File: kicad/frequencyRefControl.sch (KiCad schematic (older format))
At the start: 15 parts, among them J83 Conn_01x01_Male, J84 Conn_01x01_Male, J85 Conn_01x01_Male

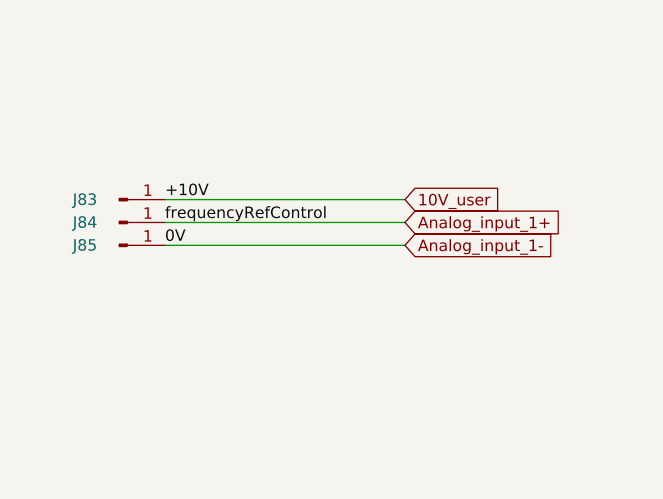
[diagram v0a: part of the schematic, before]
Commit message: KICAD: Agregar cambios esquemáticos
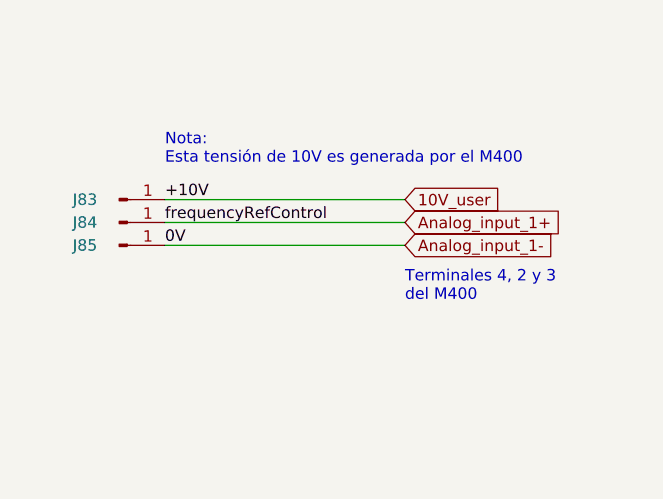
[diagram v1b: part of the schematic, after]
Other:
- note added: "Nota:\nEsta tensión de 10V es generada por el M400"
- note added: "Terminales 4, 2 y 3 \ndel M400"
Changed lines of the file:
@@
 Sheet 18 22
 Title "Mainet-mega -- frequencyRefControl"
-Date "2021-04-07"
+Date "2021-06-18"
 Rev "1.0"
 Comp "Tovenca"
@@
 Wire Wire Line
 	9050 3650 10100 3650
+Text Notes 10100 3900 0    50   ~ 0
+Terminales 4, 2 y 3 \ndel M400
+Text Notes 9050 3300 0    50   ~ 0
+Nota:\nEsta tensión de 10V es generada por el M400
 $EndSCHEMATC

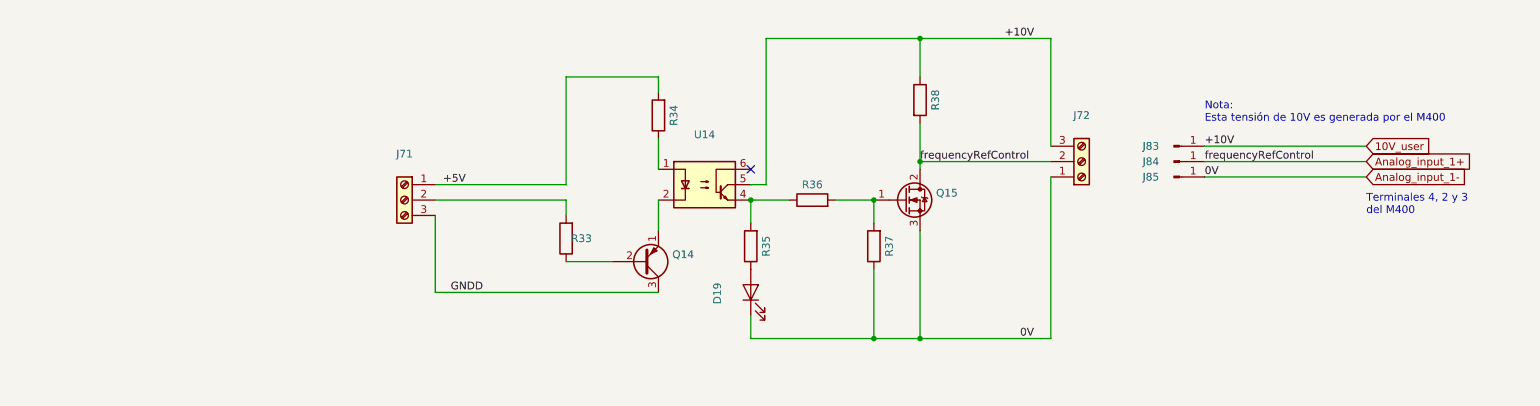
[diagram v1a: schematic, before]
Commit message: KICAD: Guardar cambios sch del control de frecuencia M400
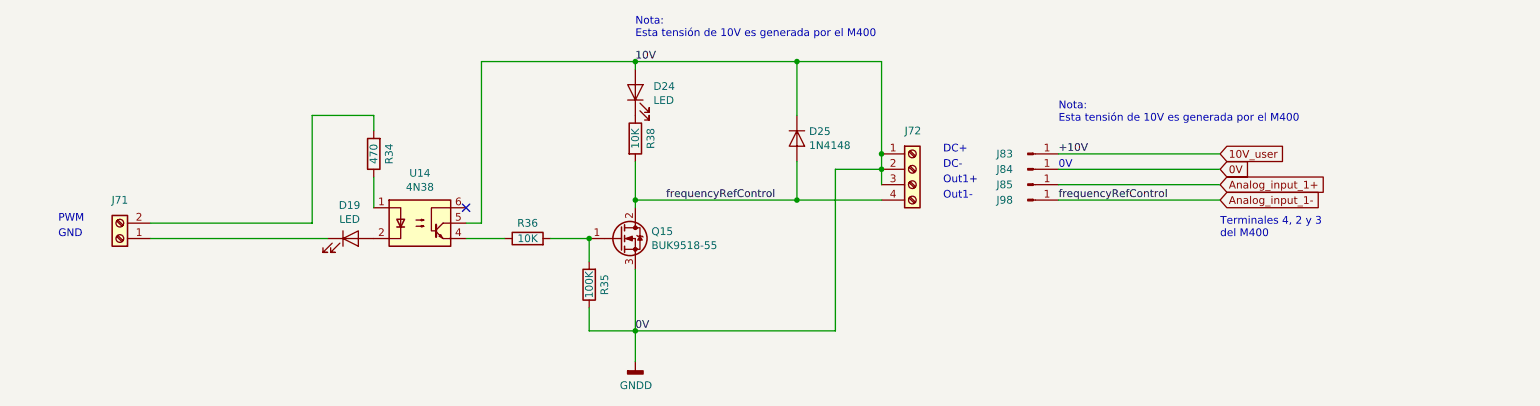
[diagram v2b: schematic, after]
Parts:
- removed J71, J72: ~, TerminalBlock_Altech:Altech_AK300_1x03_P5.00mm_45-Degree, symbol Connector:Screw_Terminal_01x03
- removed Q14: ~, Package_TO_SOT_THT:TO-92_Inline, symbol Transistor_BJT:2N3906
- removed R33, R37: ~, Resistor_THT:R_Axial_DIN0207_L6.3mm_D2.5mm_P7.62mm_Horizontal, symbol Device:R
- added D24: LED, symbol Device:LED
- added D25: 1N4148, Diode_THT:D_DO-35_SOD27_P7.62mm_Horizontal, symbol Diode:1N4148
- added J71: Screw_Terminal_01x02, symbol Connector:Screw_Terminal_01x02
- added J72: Screw_Terminal_01x04, symbol Connector:Screw_Terminal_01x04
- added J98: Conn_01x01_Male, symbol Connector:Conn_01x01_Male
- D19: value ~ -> LED; footprint LED_THT:LED_D5.0mm -> (none)
- Q15: value ~ -> BUK9518-55
- R34: value ~ -> 470; footprint Resistor_THT:R_Axial_DIN0207_L6.3mm_D2.5mm_P7.62mm_Horizontal -> Resistor_THT:R_Axial_DIN0414_L11.9mm_D4.5mm_P15.24mm_Horizontal
- R35: value ~ -> 100K; footprint Resistor_THT:R_Axial_DIN0207_L6.3mm_D2.5mm_P7.62mm_Horizontal -> Resistor_THT:R_Axial_DIN0414_L11.9mm_D4.5mm_P15.24mm_Horizontal
- R36: value ~ -> 10K; footprint Resistor_THT:R_Axial_DIN0207_L6.3mm_D2.5mm_P7.62mm_Horizontal -> Resistor_THT:R_Axial_DIN0414_L11.9mm_D4.5mm_P15.24mm_Horizontal
- R38: value ~ -> 10K; footprint Resistor_THT:R_Axial_DIN0207_L6.3mm_D2.5mm_P7.62mm_Horizontal -> Resistor_THT:R_Axial_DIN0207_L6.3mm_D2.5mm_P10.16mm_Horizontal
- U14: value ~ -> 4N38
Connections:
- net 10V_user: no longer R38.1, U14.5
- net Analog_input_1+: now also J85.1 (Pin_1); no longer J84.1 (Pin_1), Q15.2 (D), R38.2
- net Analog_input_1-: now also Q15.2 (D), R38.2, D25.2 (A), J72.4 (Pin_4), J98.1 (Pin_1); no longer D19.1 (K), J85.1 (Pin_1), Q15.3 (S)
- net GNDD: now also J84.1 (Pin_1), Q15.3 (S), R35.1, U14.5, D24.2 (A), D25.1 (K), J72.1 (Pin_1), J72.2 (Pin_2), J72.3 (Pin_3)
- net at Q15.1 (G), R36.2: now also R35.2
- net at U14.2: now also D19.2 (A)
- net at R36.1, U14.4: no longer R35.2
- net +5V: no longer names the net of R34.2
- net +5V: now also J71.2 (Pin_2)
- new net: D24.1 (K), R38.1
- new net: D19.1 (K), J71.1 (Pin_1)
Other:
- note added: "0V"
- note added: "DC+"
- note added: "DC-"
- note added: "GND"
- note added: "Out1+"
- note added: "Out1-"
- note added: "PWM"

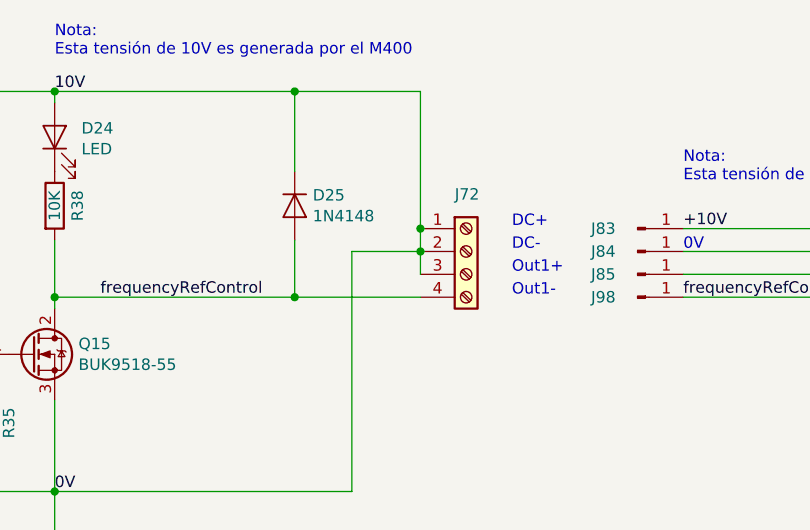
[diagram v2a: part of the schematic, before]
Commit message: KICAD: AGregar cambios en .sch del controlador de frecuencia
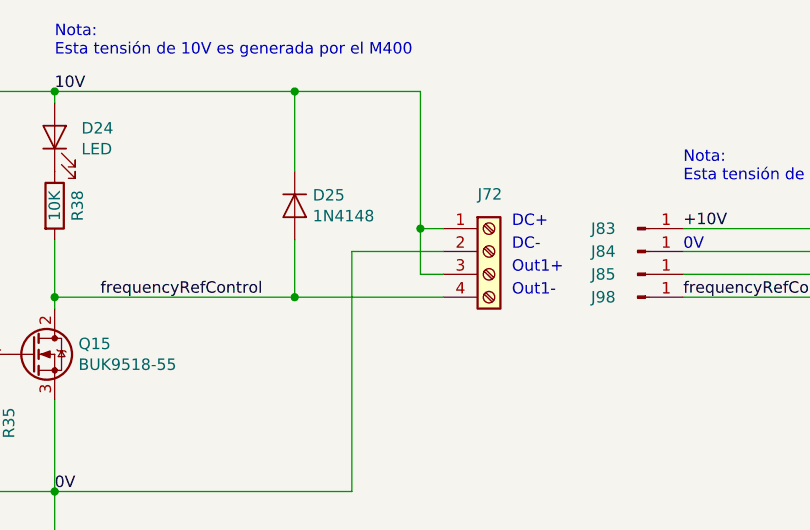
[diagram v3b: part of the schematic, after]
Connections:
- net GNDD: no longer D24.2 (A), D25.1 (K), J72.1 (Pin_1), J72.3 (Pin_3), U14.5
- new net 10V: D24.2 (A), D25.1 (K), J72.1 (Pin_1), J72.3 (Pin_3), U14.5
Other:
- moved on the sheet: J72
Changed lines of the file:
@@
 NoConn ~ 4250 3850
-Wire Wire Line
-	6950 3800 6400 3800
 Wire Wire Line
 	5350 3800 5350 3850
@@
 L Connector:Screw_Terminal_01x04 J?
 U 1 1 60DF1363
-P 7150 3600
+P 7250 3600
 AR Path="/5FC3A1C1/60DF1363" Ref="J?"  Part="1"
 AR Path="/5FBD1D9A/601C4CB6/60DF1363" Ref="J72"  Part="1"
-F 0 "J72" H 7100 3850 50  0000 L CNN
-F 1 "Screw_Terminal_01x04" H 7230 3501 50  0001 L CNN
-F 2 "" H 7150 3600 50  0001 C CNN
-F 3 "~" H 7150 3600 50  0001 C CNN
-	1    7150 3600
+F 0 "J72" H 7200 3850 50  0000 L CNN
+F 1 "Screw_Terminal_01x04" H 7330 3501 50  0001 L CNN
+F 2 "" H 7250 3600 50  0001 C CNN
+F 3 "~" H 7250 3600 50  0001 C CNN
+	1    7250 3600
 	1    0    0    -1
 $EndComp
@@
 Wire Wire Line
 	5350 2900 6400 2900
-Wire Wire Line
-	6950 2900 6950 3500
 Connection ~ 5350 2900
 Wire Wire Line
-	6950 3600 6650 3600
-Wire Wire Line
 	6650 3600 6650 4650
 Wire Wire Line
 	5350 4650 6650 4650
-Connection ~ 6950 3500
-Wire Wire Line
-	6950 3500 6950 3600
 Text Notes 7350 3500 0    50   ~ 0
 DC+
@@
 Wire Wire Line
 	8100 3600 9150 3600
-Connection ~ 6950 3600
 Wire Wire Line
 	6950 3600 6950 3700
 Text Notes 8100 3600 0    50   ~ 0
 0V
+Wire Wire Line
+	6950 2900 6950 3500
+Wire Wire Line
+	7050 3500 6950 3500
+Connection ~ 6950 3500
+Wire Wire Line
+	6950 3500 6950 3600
+Wire Wire Line
+	6650 3600 7050 3600
+Wire Wire Line
+	6950 3700 7050 3700
+Wire Wire Line
+	6400 3800 7050 3800
 $EndSCHEMATC

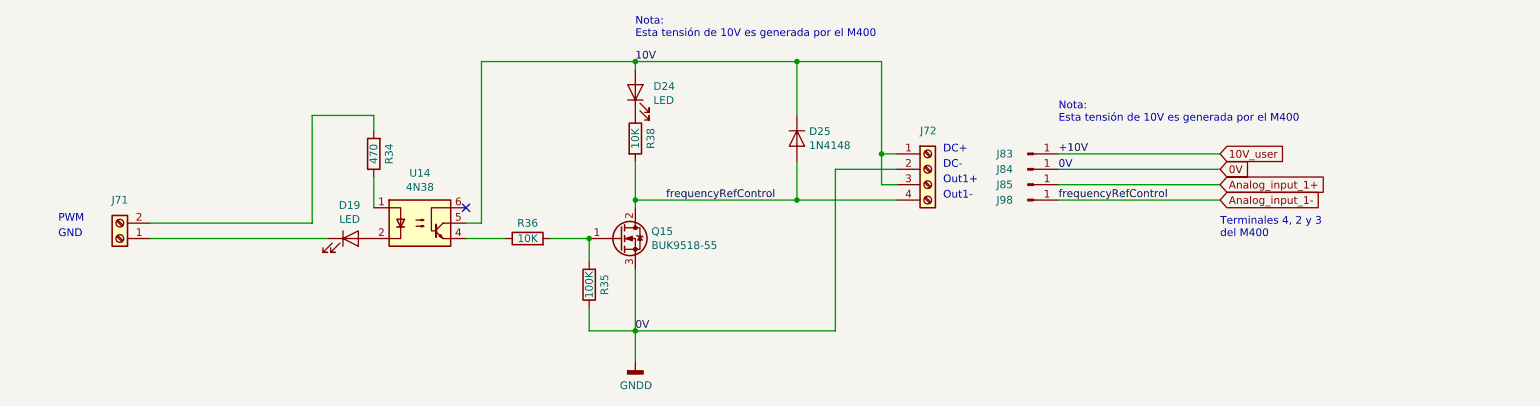
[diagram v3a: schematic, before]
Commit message: KICAD: Agregar cambios a  .sch
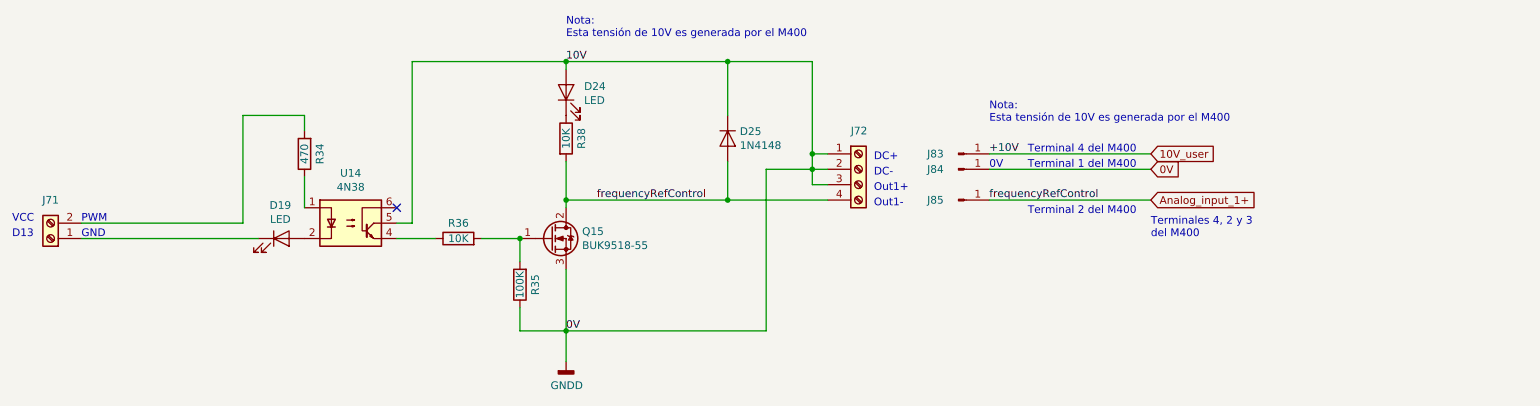
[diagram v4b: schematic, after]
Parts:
- removed J98: Conn_01x01_Male, symbol Connector:Conn_01x01_Male
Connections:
- net 10V is gone; now on net GNDD: D24.2 (A), D25.1 (K), J72.1 (Pin_1), J72.3 (Pin_3), U14.5
- net Analog_input_1- is gone; now on net Analog_input_1+: D25.2 (A), J72.4 (Pin_4), Q15.2 (D), R38.2
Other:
- note added: "D13"
- note added: "Terminal 1 del M400"
- note added: "Terminal 2 del M400"
- note added: "Terminal 4 del M400"
- note added: "VCC"
- moved on the sheet: D19, D24, D25, J71, J72, J83, J84, J85, Q15, R34, R35, R36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

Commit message: KICAD: Guardar cambios .sch frequencyRefControl
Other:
- note added: "D13 (frequencyRefControl)"
- note removed: "D13"
- moved on the sheet: D19, D24, D25, J71, J72, J83, J84, J85, Q15, R34, R35, R36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
